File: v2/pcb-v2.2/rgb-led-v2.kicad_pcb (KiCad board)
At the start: 2 copper layers, 90 x 50 mm, 15 parts, among them CON1 BARREL_JACK, SW1 SPST

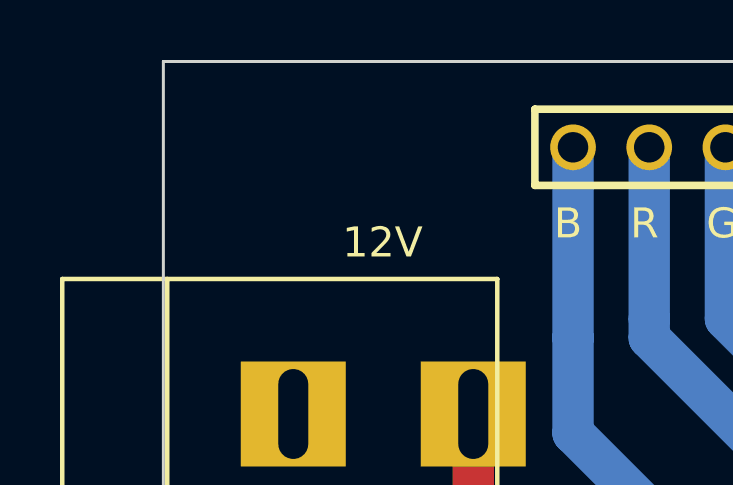
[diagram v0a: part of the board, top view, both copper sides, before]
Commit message: Add another mounting hole
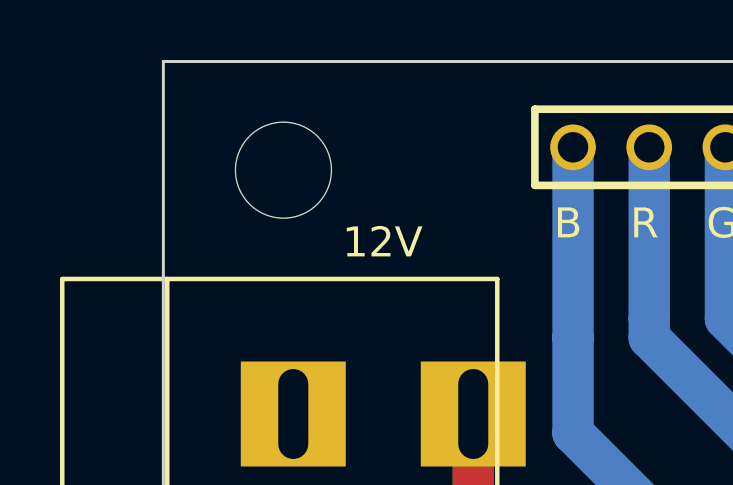
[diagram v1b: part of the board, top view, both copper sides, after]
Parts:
- added REF**: MountingHole_3.2mm_M3, Mounting_Holes:MountingHole_3.2mm_M3, F.Cu at (22.7, 23.6)
- moved G*** 0.92 mm to (38.5, 30.1)
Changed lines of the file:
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@@
     (tracks 83)
     (zones 0)
-    (modules 15)
+    (modules 16)
     (nets 35)
   )
@@
     (add_net "Net-(UC1-Pad9)")
   )
+  (module Mounting_Holes:MountingHole_3.2mm_M3 (layer F.Cu)
+    (at 22.733 23.622)
+    (descr "Mounting Hole 3.2mm, no annular, M3")
+    (tags "mounting hole 3.2mm no annular m3")
+    (fp_text reference REF** (at 0 -4.2) (layer F.SilkS) hide
+      (effects (font (size 1 1) (thickness 0.15)))
+    )
+    (fp_text value MountingHole_3.2mm_M3 (at 0 4.2) (layer F.Fab)
+      (effects (font (size 1 1) (thickness 0.15)))
+    )
+    (fp_circle (center 0 0) (end 3.2 0) (layer Cmts.User) (width 0.15))
+    (fp_circle (center 0 0) (end 3.45 0) (layer F.CrtYd) (width 0.05))
+    (pad 1 np_thru_hole circle (at 0 0) (size 3.2 3.2) (drill 3.2) (layers *.Cu *.Mask F.SilkS))
+  )
   (module KCD3 (layer F.Cu)
     (at 29.21 67.31 90)
@@
   )
   (module OSHW_MASK_7MM (layer F.Cu)
-    (at 38.735 29.21)
+    (at 38.481 30.099)
     (fp_text reference G*** (at 0 3.71094) (layer F.Mask) hide
       (effects (font (size 0.3175 0.3175) (thickness 0.0635)))
@@
     (effects (font (size 1 1) (thickness 0.15)))
   )
-  (gr_text "open source\nhardware" (at 38.735 34.29) (layer F.Mask)
+  (gr_text "open source\nhardware" (at 38.481 35.179) (layer F.Mask)
     (effects (font (size 1.4 1.4) (thickness 0.25)))
   )
